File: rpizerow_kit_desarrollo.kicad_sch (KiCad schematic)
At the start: 18 parts, among them J1 Conector USB, J2 Screw_Terminal_01x02, SW1 SW_DIP_x01, U1 RPizeroW, U2 ADS1115IDGS, U3 BMP180, U4 TM1637

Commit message: agrego huella a rgb
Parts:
- D1: footprint (none) -> LED_THT:LED_D5.0mm-4_RGB
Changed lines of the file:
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@@
       (effects (font (size 1.27 1.27)))
     )
-    (property "Footprint" "" (at 131.445 41.91 0)
+    (property "Footprint" "LED_THT:LED_D5.0mm-4_RGB" (at 131.445 41.91 0)
       (effects (font (size 1.27 1.27)) hide)
     )

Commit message: corrijo RGB
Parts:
- removed D1: LED_GKBR, LED_THT:LED_D5.0mm-4_RGB, symbol Device:LED_GKBR
- added D1: LED_RKGB, symbol Device:LED_RKGB
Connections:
- net GND: now also D1.2 (K)
- net PWM 1: now also R4.1; no longer R3.1
- net PWM 2: now also R3.1; no longer R4.1
- net at R4.2: now also D1.3 (GA)
- net at R3.2: now also D1.1 (RA)
- net at R5.2: now also D1.4 (BA)
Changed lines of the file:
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@@
     (stroke (width 0) (type default))
   )
-  (wire (pts (xy 172.085 82.55) (xy 180.975 82.55))
+  (wire (pts (xy 177.165 82.55) (xy 180.975 82.55))
     (stroke (width 0) (type default))
   )
@@
     )
   )
-  (global_label "PWM 1" (shape input) (at 113.665 38.1 180) (fields_autoplaced)
+  (global_label "PWM 2" (shape input) (at 113.665 38.1 180) (fields_autoplaced)
     (effects (font (size 1.27 1.27)) (justify right))
     (property "Intersheetrefs" "${INTERSHEET_REFS}" (at 104.4093 38.1 0)
@@
     )
   )
-  (global_label "PWM 2" (shape input) (at 113.665 43.18 180) (fields_autoplaced)
+  (global_label "PWM 1" (shape input) (at 113.665 43.18 180) (fields_autoplaced)
     (effects (font (size 1.27 1.27)) (justify right))
     (property "Intersheetrefs" "${INTERSHEET_REFS}" (at 104.4093 43.18 0)
@@
     )
   )
-  (global_label "CLK" (shape input) (at 172.085 82.55 180) (fields_autoplaced)
-    (effects (font (size 1.27 1.27)) (justify right))
-    (property "Intersheetrefs" "${INTERSHEET_REFS}" (at 165.6111 82.55 0)
+  (global_label "CLK" (shape input) (at 177.165 82.55 180) (fields_autoplaced)
+    (effects (font (size 1.27 1.27)) (justify right))
+    (property "Intersheetrefs" "${INTERSHEET_REFS}" (at 170.6911 82.55 0)
       (effects (font (size 1.27 1.27)) (justify right) hide)
     )
@@
         (path "/e687ab57-d0b0-4656-9edc-b34788e5e6b0"
           (reference "#PWR08") (unit 1)
-        )
-      )
-    )
-  )
-  (symbol (lib_id "Device:LED_GKBR") (at 131.445 43.18 180) (unit 1)
-    (in_bom yes) (on_board yes) (dnp no)
-    (property "Reference" "D1" (at 131.445 55.88 0)
-      (effects (font (size 1.27 1.27)))
-    )
-    (property "Value" "LED_GKBR" (at 131.445 53.34 0)
-      (effects (font (size 1.27 1.27)))
-    )
-    (property "Footprint" "LED_THT:LED_D5.0mm-4_RGB" (at 131.445 41.91 0)
-      (effects (font (size 1.27 1.27)) hide)
-    )
-    (property "Datasheet" "~" (at 131.445 41.91 0)
-      (effects (font (size 1.27 1.27)) hide)
-    )
-    (pin "1")
-    (pin "2")
-    (pin "3")
-    (pin "4")
-    (instances
-      (project "rpizerow_kit_desarrollo"
-        (path "/e687ab57-d0b0-4656-9edc-b34788e5e6b0"
-          (reference "D1") (unit 1)
         )
       )
@@
         )
       )
+    )
+  )
+  (symbol (lib_id "Device:LED_RKGB") (at 131.445 43.18 0) (mirror y) (unit 1)
+    (in_bom yes) (on_board yes) (dnp no) (fields_autoplaced)
+    (property "Reference" "D1" (at 131.445 30.48 0)
+      (effects (font (size 1.27 1.27)))
+    )
+    (property "Value" "LED_RKGB" (at 131.445 33.02 0)
+      (effects (font (size 1.27 1.27)))
+    )
+    (property "Footprint" "" (at 131.445 44.45 0)
+      (effects (font (size 1.27 1.27)) hide)
+    )
+    (property "Datasheet" "~" (at 131.445 44.45 0)
+      (effects (font (size 1.27 1.27)) hide)
+    )
+    (pin "1")
+    (pin "2")
+    (pin "3")
+    (pin "4")
+    (instances
+      (project "rpizerow_kit_desarrollo"
+        (path "/e687ab57-d0b0-4656-9edc-b34788e5e6b0"
+          (reference "D1") (unit 1)
+        )
+      )

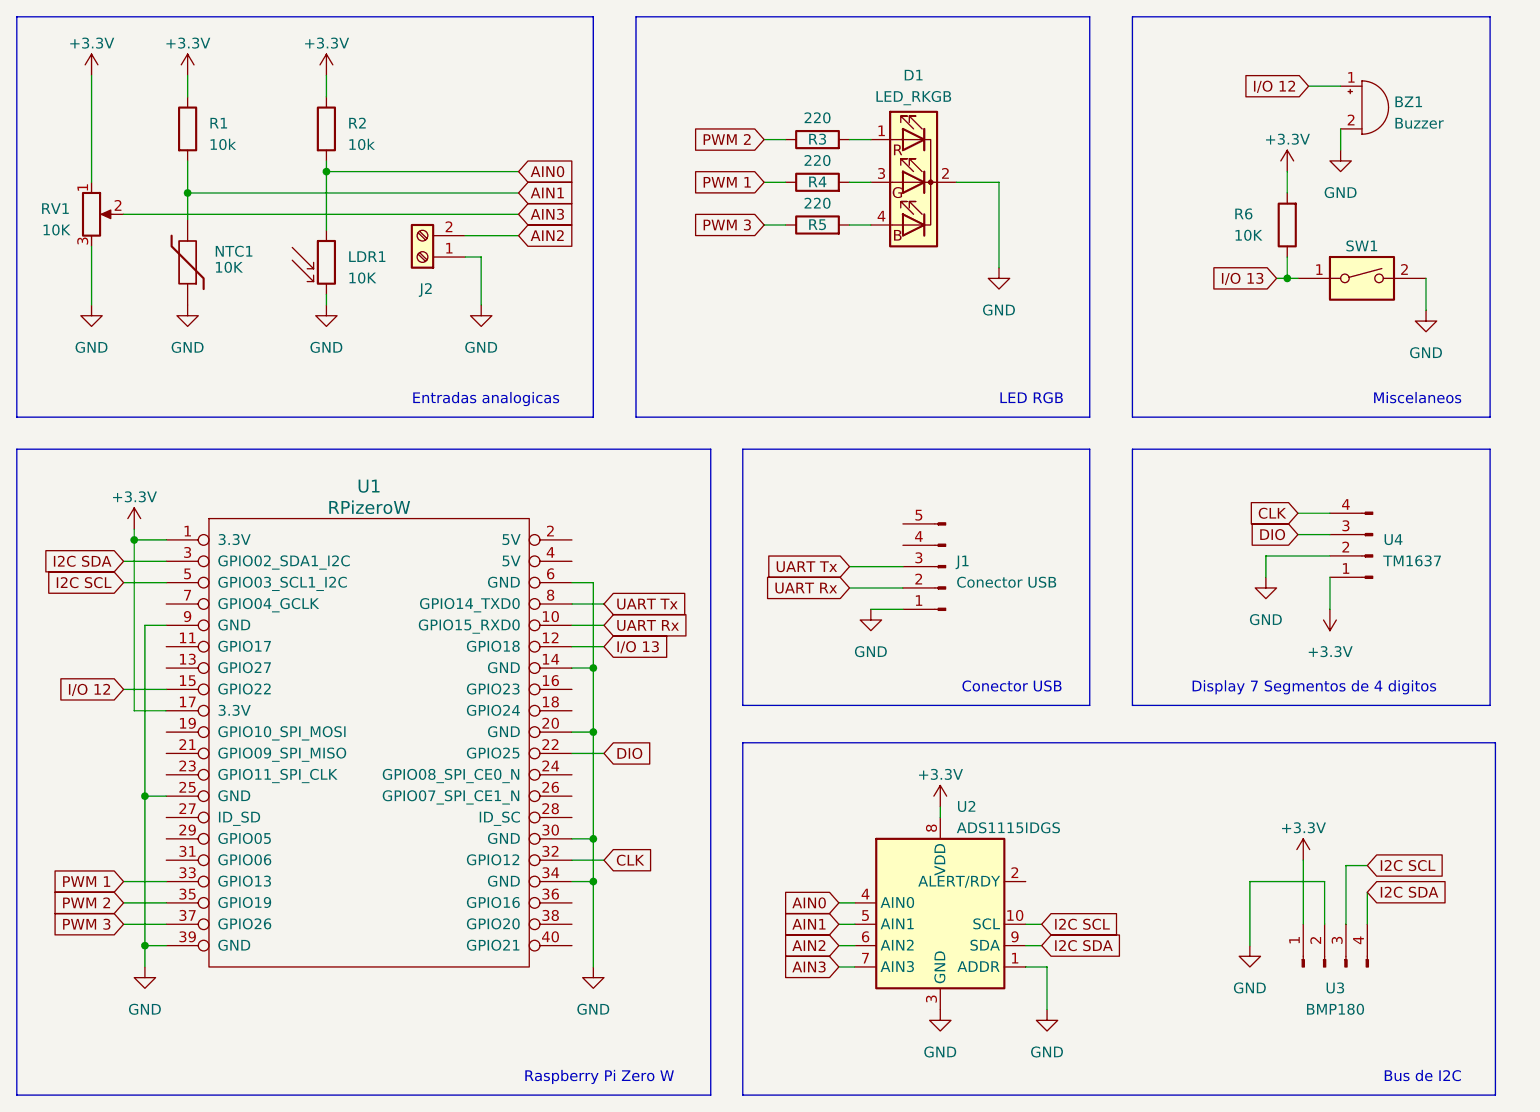
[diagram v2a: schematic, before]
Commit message: corrijo etiquetas
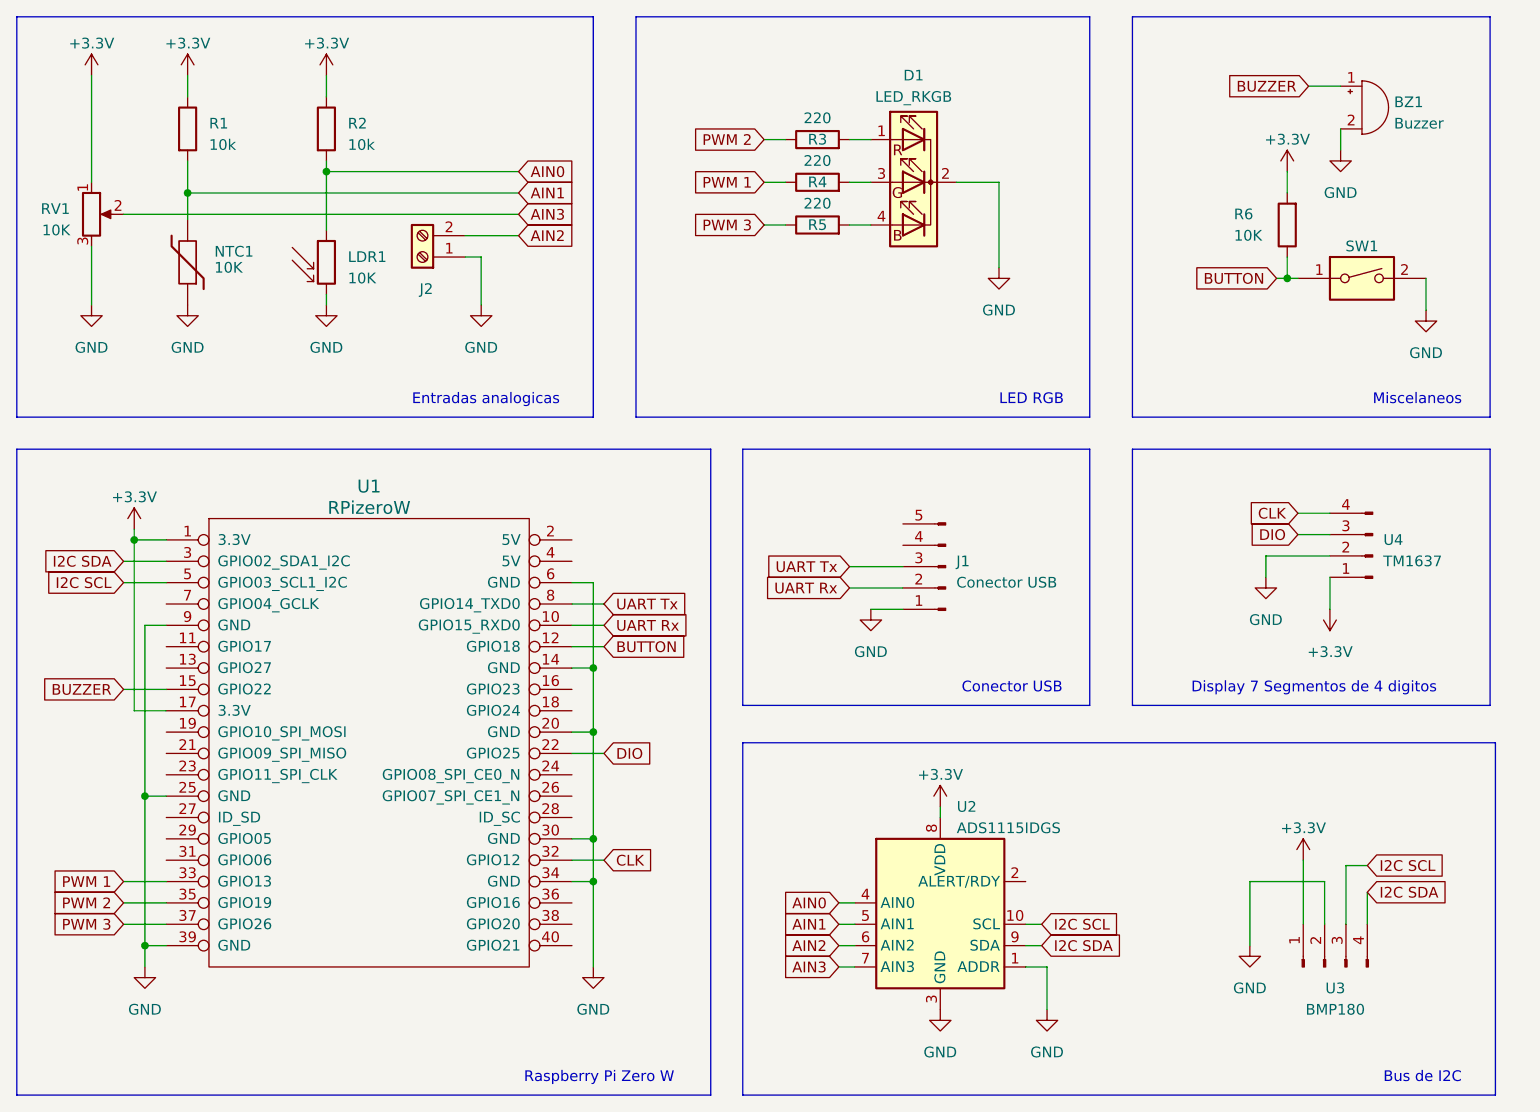
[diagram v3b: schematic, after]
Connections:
- net I/O 12 renamed BUZZER
- net I/O 13 renamed BUTTON
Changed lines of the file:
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@@
     )
   )
-  (global_label "I{slash}O 13" (shape input) (at 94.615 98.425 0) (fields_autoplaced)
+  (global_label "BUTTON" (shape input) (at 94.615 98.425 0) (fields_autoplaced)
     (effects (font (size 1.27 1.27)) (justify left))
-    (property "Intersheetrefs" "${INTERSHEET_REFS}" (at 104.1732 98.425 0)
+    (property "Intersheetrefs" "${INTERSHEET_REFS}" (at 104.7175 98.425 0)
       (effects (font (size 1.27 1.27)) (justify left) hide)
     )
@@
     )
   )
-  (global_label "I{slash}O 12" (shape input) (at 37.465 103.505 180) (fields_autoplaced)
+  (global_label "BUZZER" (shape input) (at 37.465 103.505 180) (fields_autoplaced)
     (effects (font (size 1.27 1.27)) (justify right))
-    (property "Intersheetrefs" "${INTERSHEET_REFS}" (at 27.9068 103.505 0)
+    (property "Intersheetrefs" "${INTERSHEET_REFS}" (at 27.1207 103.505 0)
       (effects (font (size 1.27 1.27)) (justify right) hide)
     )
@@
     )
   )
-  (global_label "I{slash}O 12" (shape input) (at 178.435 31.75 180) (fields_autoplaced)
+  (global_label "BUZZER" (shape input) (at 178.435 31.75 180) (fields_autoplaced)
     (effects (font (size 1.27 1.27)) (justify right))
-    (property "Intersheetrefs" "${INTERSHEET_REFS}" (at 168.8768 31.75 0)
+    (property "Intersheetrefs" "${INTERSHEET_REFS}" (at 168.0907 31.75 0)
       (effects (font (size 1.27 1.27)) (justify right) hide)
     )
   )
-  (global_label "I{slash}O 13" (shape input) (at 174.625 54.61 180) (fields_autoplaced)
+  (global_label "BUTTON" (shape input) (at 174.625 54.61 180) (fields_autoplaced)
     (effects (font (size 1.27 1.27)) (justify right))
-    (property "Intersheetrefs" "${INTERSHEET_REFS}" (at 165.0668 54.61 0)
+    (property "Intersheetrefs" "${INTERSHEET_REFS}" (at 164.5225 54.61 0)
       (effects (font (size 1.27 1.27)) (justify right) hide)
     )

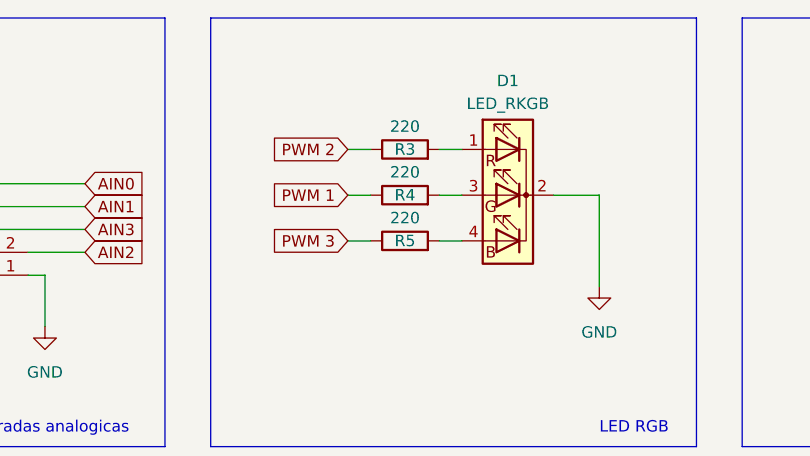
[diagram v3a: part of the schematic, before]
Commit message: corrijo valor de resistencias
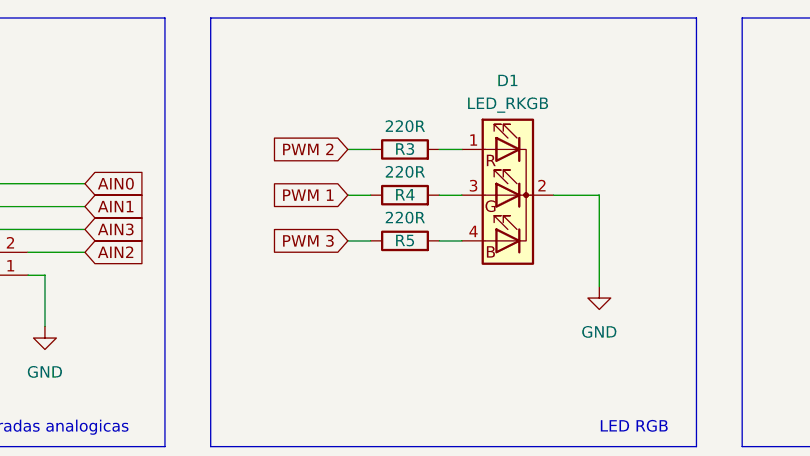
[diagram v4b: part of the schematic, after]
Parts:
- R3, R4, R5: value 220 -> 220R
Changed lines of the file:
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@@
       (effects (font (size 1.27 1.27)))
     )
-    (property "Value" "220" (at 120.015 40.64 90)
+    (property "Value" "220R" (at 120.015 40.64 90)
       (effects (font (size 1.27 1.27)))
     )
@@
       (effects (font (size 1.27 1.27)))
     )
-    (property "Value" "220" (at 120.015 45.72 90)
+    (property "Value" "220R" (at 120.015 45.72 90)
       (effects (font (size 1.27 1.27)))
     )
@@
       (effects (font (size 1.27 1.27)))
     )
-    (property "Value" "220" (at 120.015 35.56 90)
-      (effects (font (size 1.27 1.27)))
-    )
+    (property "Value" "220R" (at 120.015 35.56 90)
+      (effects (font (size 1.27 1.27)))
+    )
